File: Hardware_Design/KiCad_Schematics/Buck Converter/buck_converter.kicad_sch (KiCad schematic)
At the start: 3 parts, among them J1 Conn_01x02_Socket, J2 Conn_01x02_Socket, J3 Conn_01x01_Pin

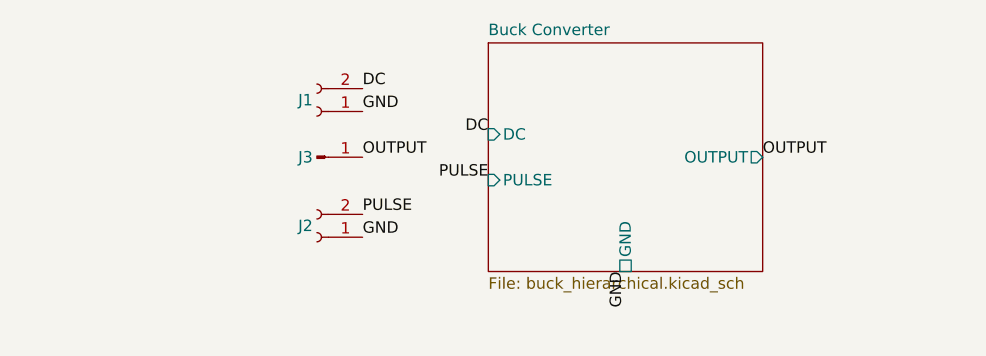
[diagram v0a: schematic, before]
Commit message: Add simulation circuit for Buck Converter
Added the simulation circuit to analyze the output graphs, but the expected waveform/results are not yet achieved.
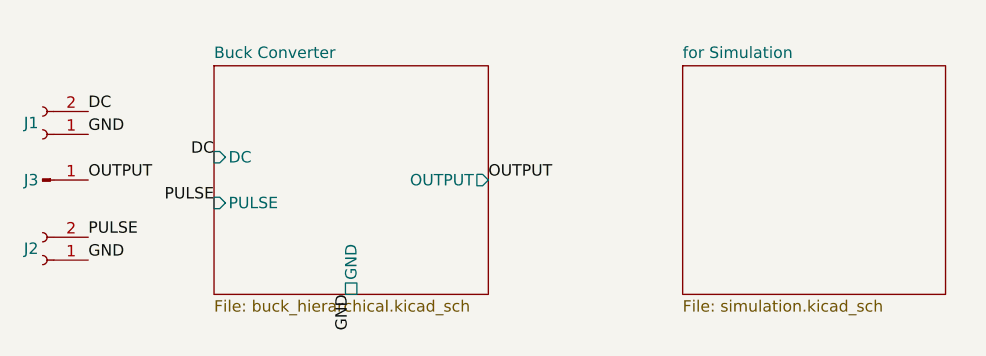
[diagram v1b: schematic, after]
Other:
- added sheet for Simulation (simulation.kicad_sch)
- moved on the sheet: J1, J2, J3
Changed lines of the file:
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@@
 	(paper "A4")
 	(label "GND"
-		(at 111.76 96.52 0)
+		(at 81.28 99.06 0)
 		(effects
 			(font
@@
 	)
 	(label "OUTPUT"
-		(at 111.76 101.6 0)
+		(at 81.28 104.14 0)
 		(effects
 			(font
@@
 	)
 	(label "GND"
-		(at 140.97 114.3 270)
+		(at 110.49 116.84 270)
 		(effects
 			(font
@@
 	)
 	(label "DC"
-		(at 111.76 93.98 0)
+		(at 81.28 96.52 0)
 		(effects
 			(font
@@
 	)
 	(label "PULSE"
-		(at 111.76 107.95 0)
+		(at 81.28 110.49 0)
 		(effects
 			(font
@@
 	)
 	(label "GND"
-		(at 111.76 110.49 0)
+		(at 81.28 113.03 0)
 		(effects
 			(font
@@
 	)
 	(label "OUTPUT"
-		(at 156.21 101.6 0)
+		(at 125.73 104.14 0)
 		(effects
 			(font
@@
 	)
 	(label "DC"
-		(at 125.73 99.06 180)
+		(at 95.25 101.6 180)
 		(effects
 			(font
@@
 	)
 	(label "PULSE"
-		(at 125.73 104.14 180)
+		(at 95.25 106.68 180)
 		(effects
 			(font
@@
 	(symbol
 		(lib_id "Connector:Conn_01x02_Socket")
-		(at 106.68 96.52 180)
+		(at 76.2 99.06 180)
 		(unit 1)
 		(body_style 1)
@@
 		(dnp no)
 		(property "Reference" "J1"
-			(at 105.41 95.25 0)
+			(at 74.93 97.79 0)
 			(show_name no)
 			(do_not_autoplace no)
@@
 		)
 		(property "Value" "Conn_01x02_Socket"
-			(at 107.315 91.44 0)
+			(at 76.835 93.98 0)
 			(hide yes)
 			(show_name no)
@@
 		)
 		(property "Footprint" "Connector_PinSocket_2.54mm:PinSocket_1x02_P2.54mm_Vertical"
-			(at 106.68 96.52 0)
+			(at 76.2 99.06 0)
 			(hide yes)
 			(show_name no)
@@
 		)
 		(property "Datasheet" ""
-			(at 106.68 96.52 0)
+			(at 76.2 99.06 0)
 			(hide yes)
 			(show_name no)
@@
 		)
 		(property "Description" "Generic connector, single row, 01x02, script generated"
-			(at 106.68 96.52 0)
+			(at 76.2 99.06 0)
 			(hide yes)
 			(show_name no)
@@
 	(symbol
 		(lib_id "Connector:Conn_01x01_Pin")
-		(at 106.68 101.6 0)
+		(at 76.2 104.14 0)
 		(unit 1)
 		(body_style 1)
@@
 		(dnp no)
 		(property "Reference" "J3"
-			(at 105.41 101.6 0)
+			(at 74.93 104.14 0)
 			(show_name no)
 			(do_not_autoplace no)
@@
 		)
 		(property "Value" "Conn_01x01_Pin"
-			(at 107.315 99.06 0)
+			(at 76.835 101.6 0)
 			(hide yes)
 			(show_name no)
@@
 		)
 		(property "Footprint" "Connector_PinHeader_2.54mm:PinHeader_1x01_P2.54mm_Vertical"
-			(at 106.68 101.6 0)
+			(at 76.2 104.14 0)
 			(hide yes)
 			(show_name no)
@@
 		)
 		(property "Datasheet" ""
-			(at 106.68 101.6 0)
+			(at 76.2 104.14 0)
 			(hide yes)
 			(show_name no)
@@
 		)
 		(property "Description" "Generic connector, single row, 01x01, script generated"
-			(at 106.68 101.6 0)
+			(at 76.2 104.14 0)
 			(hide yes)
 			(show_name no)
@@
 	(symbol
 		(lib_id "Connector:Conn_01x02_Socket")
-		(at 106.68 110.49 180)
+		(at 76.2 113.03 180)
 		(unit 1)
 		(body_style 1)
@@
 		(dnp no)
 		(property "Reference" "J2"
-			(at 105.41 109.22 0)
+			(at 74.93 111.76 0)
 			(show_name no)
 			(do_not_autoplace no)
@@
 		)
 		(property "Value" "Conn_01x02_Socket"
-			(at 107.315 105.41 0)
+			(at 76.835 107.95 0)
 			(hide yes)
 			(show_name no)
@@
 		)
 		(property "Footprint" "Connector_PinSocket_2.54mm:PinSocket_1x02_P2.54mm_Vertical"
-			(at 106.68 110.49 0)
+			(at 76.2 113.03 0)
 			(hide yes)
 			(show_name no)
@@
 		)
 		(property "Datasheet" ""
-			(at 106.68 110.49 0)
+			(at 76.2 113.03 0)
 			(hide yes)
 			(show_name no)
@@
 		)
 		(property "Description" "Generic connector, single row, 01x02, script generated"
-			(at 106.68 110.49 0)
+			(at 76.2 113.03 0)
 			(hide yes)
 			(show_name no)
@@
 	)
 	(sheet
-		(at 125.73 88.9)
+		(at 147.32 91.44)
+		(size 29.21 25.4)
+		(exclude_from_sim no)
+		(in_bom no)
+		(on_board no)
+		(dnp no)
+		(fields_autoplaced yes)
+		(stroke
+			(width 0.1524)
+			(type solid)
+			(color 194 0 0 1)
+		)
+		(fill
+			(color 0 0 0 0)
+		)
+		(property "Sheetname" "for Simulation"
+			(at 147.32 90.7284 0)
+			(show_name no)
+			(do_not_autoplace no)
+			(effects
+				(font
+					(size 1.27 1.27)
+				)
+				(justify left bottom)
+			)
+		)
+		(property "Sheetfile" "simulation.kicad_sch"
+			(at 147.32 117.4246 0)
+			(show_name no)
+			(do_not_autoplace no)
+			(effects
+				(font
+					(size 1.27 1.27)
+				)
+				(justify left top)
+			)
+		)
+		(instances
+			(project "buck_converter"
+				(path "/e6ad1407-9765-4ff4-965d-dd4ca2472230"
+					(page "3")
+				)
+			)
+		)
+	)
+	(sheet
+		(at 95.25 91.44)
 		(size 30.48 25.4)
 		(exclude_from_sim no)
@@
 		)
 		(property "Sheetname" "Buck Converter"
-			(at 125.73 88.1884 0)
+			(at 95.25 90.7284 0)
 			(show_name no)
 			(do_not_autoplace no)
@@
 		)
 		(property "Sheetfile" "buck_hierarchical.kicad_sch"
-			(at 125.73 114.8846 0)
+			(at 95.25 117.4246 0)
 			(show_name no)
 			(do_not_autoplace no)
@@
 		)
 		(pin "DC" input
-			(at 125.73 99.06 180)
+			(at 95.25 101.6 180)
 			(effects
 				(font
@@
 		)
 		(pin "OUTPUT" output
-			(at 156.21 101.6 0)
+			(at 125.73 104.14 0)
 			(effects
 				(font
@@
 		)
 		(pin "PULSE" input
-			(at 125.73 104.14 180)
+			(at 95.25 106.68 180)
 			(effects
 				(font
@@
 		)
 		(pin "GND" passive
-			(at 140.97 114.3 270)
-			(effects
-				(font
+			(at 110.49 116.84 270)
+			(effects
+				(font

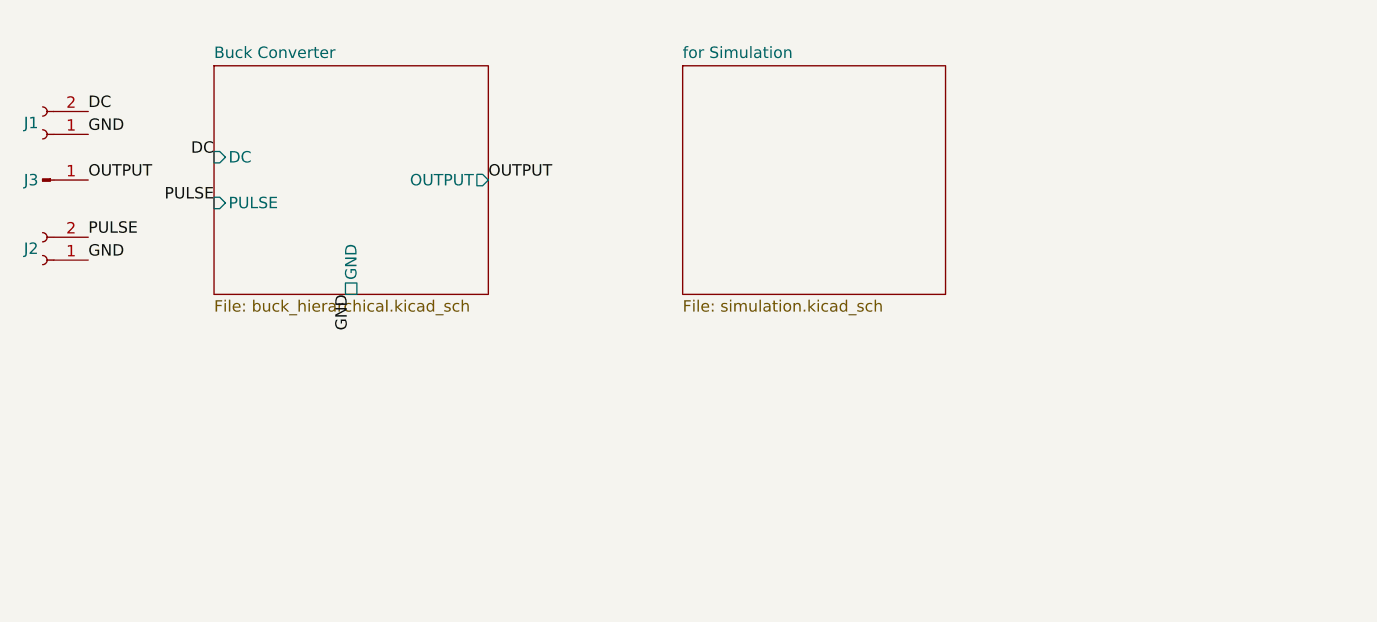
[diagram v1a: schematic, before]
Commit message: init: initialize new circuit for the previous problem
Started the Bootstrap Driver circuit to solve the previous problem. This way, the NMOSFET will be able to operate in full saturation.
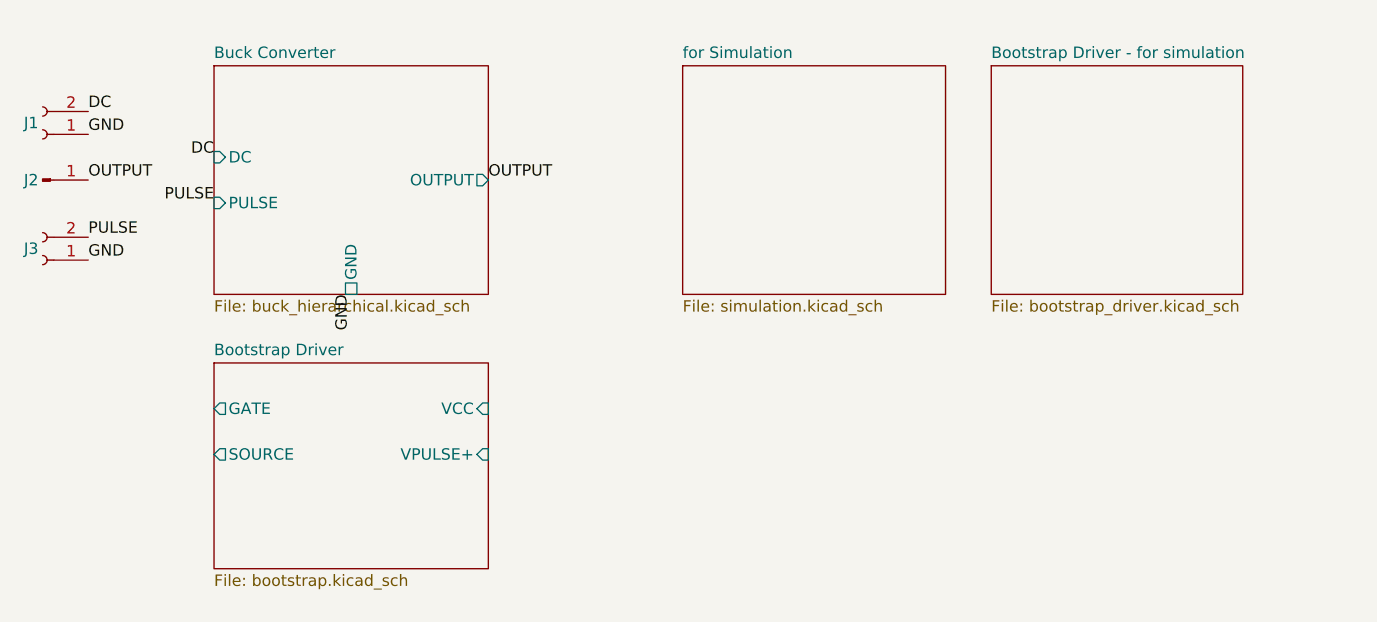
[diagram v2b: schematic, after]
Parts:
- renumbered J3 to J2, J2 to J3
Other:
- added sheet Bootstrap Driver (bootstrap.kicad_sch)
- added sheet Bootstrap Driver - for simulation (bootstrap_driver.kicad_sch)
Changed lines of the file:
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@@
 		(unit 1)
 		(body_style 1)
-		(exclude_from_sim no)
+		(exclude_from_sim yes)
 		(in_bom yes)
 		(on_board yes)
@@
 		(unit 1)
 		(body_style 1)
-		(exclude_from_sim no)
+		(exclude_from_sim yes)
 		(in_bom yes)
 		(on_board yes)
 		(in_pos_files yes)
 		(dnp no)
-		(property "Reference" "J3"
+		(property "Reference" "J2"
 			(at 74.93 104.14 0)
 			(show_name no)
@@
 			(project "buck_converter"
 				(path "/e6ad1407-9765-4ff4-965d-dd4ca2472230"
-					(reference "J3")
+					(reference "J2")
 					(unit 1)
 				)
@@
 		(unit 1)
 		(body_style 1)
+		(exclude_from_sim yes)
+		(in_bom yes)
+		(on_board yes)
+		(in_pos_files yes)
+		(dnp no)
+		(property "Reference" "J3"
+			(at 74.93 111.76 0)
+			(show_name no)
+			(do_not_autoplace no)
+			(effects
+				(font
+					(size 1.27 1.27)
+				)
+			)
+		)
+		(property "Value" "Conn_01x02_Socket"
+			(at 76.835 107.95 0)
+			(hide yes)
+			(show_name no)
+			(do_not_autoplace no)
+			(effects
+				(font
+					(size 1.27 1.27)
+				)
+			)
+		)
+		(property "Footprint" "Connector_PinSocket_2.54mm:PinSocket_1x02_P2.54mm_Vertical"
+			(at 76.2 113.03 0)
+			(hide yes)
+			(show_name no)
+			(do_not_autoplace no)
+			(effects
+				(font
+					(size 1.27 1.27)
+				)
+			)
+		)
+		(property "Datasheet" ""
+			(at 76.2 113.03 0)
+			(hide yes)
+			(show_name no)
+			(do_not_autoplace no)
+			(effects
+				(font
+					(size 1.27 1.27)
+				)
+			)
+		)
+		(property "Description" "Generic connector, single row, 01x02, script generated"
+			(at 76.2 113.03 0)
+			(hide yes)
+			(show_name no)
+			(do_not_autoplace no)
+			(effects
+				(font
+					(size 1.27 1.27)
+				)
+			)
+		)
+		(pin "2"
+		)
+		(pin "1"
+		)
+		(instances
+			(project "buck_converter"
+				(path "/e6ad1407-9765-4ff4-965d-dd4ca2472230"
+					(reference "J3")
+					(unit 1)
+				)
+			)
+		)
+	)
+	(sheet
+		(at 181.61 91.44)
+		(size 27.94 25.4)
 		(exclude_from_sim no)
 		(in_bom yes)
 		(on_board yes)
-		(in_pos_files yes)
-		(dnp no)
-		(property "Reference" "J2"
-			(at 74.93 111.76 0)
-			(show_name no)
-			(do_not_autoplace no)
-			(effects
-				(font
-					(size 1.27 1.27)
-				)
-			)
-		)
-		(property "Value" "Conn_01x02_Socket"
-			(at 76.835 107.95 0)
-			(hide yes)
-			(show_name no)
-			(do_not_autoplace no)
-			(effects
-				(font
-					(size 1.27 1.27)
-				)
-			)
-		)
-		(property "Footprint" "Connector_PinSocket_2.54mm:PinSocket_1x02_P2.54mm_Vertical"
-			(at 76.2 113.03 0)
-			(hide yes)
-			(show_name no)
-			(do_not_autoplace no)
-			(effects
-				(font
-					(size 1.27 1.27)
-				)
-			)
-		)
-		(property "Datasheet" ""
-			(at 76.2 113.03 0)
-			(hide yes)
-			(show_name no)
-			(do_not_autoplace no)
-			(effects
-				(font
-					(size 1.27 1.27)
-				)
-			)
-		)
-		(property "Description" "Generic connector, single row, 01x02, script generated"
-			(at 76.2 113.03 0)
-			(hide yes)
-			(show_name no)
-			(do_not_autoplace no)
-			(effects
-				(font
-					(size 1.27 1.27)
-				)
-			)
-		)
-		(pin "2"
-		)
-		(pin "1"
-		)
-		(instances
-			(project "buck_converter"
-				(path "/e6ad1407-9765-4ff4-965d-dd4ca2472230"
-					(reference "J2")
-					(unit 1)
+		(dnp no)
+		(fields_autoplaced yes)
+		(stroke
+			(width 0.1524)
+			(type solid)
+			(color 0 255 0 1)
+		)
+		(fill
+			(color 0 0 0 0)
+		)
+		(property "Sheetname" "Bootstrap Driver - for simulation"
+			(at 181.61 90.7284 0)
+			(show_name no)
+			(do_not_autoplace no)
+			(effects
+				(font
+					(size 1.27 1.27)
+				)
+				(justify left bottom)
+			)
+		)
+		(property "Sheetfile" "bootstrap_driver.kicad_sch"
+			(at 181.61 117.4246 0)
+			(show_name no)
+			(do_not_autoplace no)
+			(effects
+				(font
+					(size 1.27 1.27)
+				)
+				(justify left top)
+			)
+		)
+		(instances
+			(project "buck_converter"
+				(path "/e6ad1407-9765-4ff4-965d-dd4ca2472230"
+					(page "4")
 				)
 			)
@@
 			(width 0.1524)
 			(type solid)
-			(color 194 0 0 1)
+			(color 0 132 0 1)
 		)
 		(fill
@@
 				(path "/e6ad1407-9765-4ff4-965d-dd4ca2472230"
 					(page "3")
+				)
+			)
+		)
+	)
+	(sheet
+		(at 95.25 124.46)
+		(size 30.48 22.86)
+		(exclude_from_sim yes)
+		(in_bom no)
+		(on_board yes)
+		(dnp no)
+		(fields_autoplaced yes)
+		(stroke
+			(width 0.1524)
+			(type solid)
+		)
+		(fill
+			(color 0 0 0 0)
+		)
+		(property "Sheetname" "Bootstrap Driver"
+			(at 95.25 123.7484 0)
+			(show_name no)
+			(do_not_autoplace no)
+			(effects
+				(font
+					(size 1.27 1.27)
+				)
+				(justify left bottom)
+			)
+		)
+		(property "Sheetfile" "bootstrap.kicad_sch"
+			(at 95.25 147.9046 0)
+			(show_name no)
+			(do_not_autoplace no)
+			(effects
+				(font
+					(size 1.27 1.27)
+				)
+				(justify left top)
+			)
+		)
+		(pin "GATE" output
+			(at 95.25 129.54 180)
+			(effects
+				(font
+					(size 1.27 1.27)
+				)
+				(justify left)
+			)
+		)
+		(pin "SOURCE" output
+			(at 95.25 134.62 180)
+			(effects
+				(font
+					(size 1.27 1.27)
+				)
+				(justify left)
+			)
+		)
+		(pin "VCC" input
+			(at 125.73 129.54 0)
+			(effects
+				(font
+					(size 1.27 1.27)
+				)
+				(justify right)
+			)
+		)
+		(pin "VPULSE+" input
+			(at 125.73 134.62 0)
+			(effects
+				(font
+					(size 1.27 1.27)
+				)
+				(justify right)
+			)
+		)
+		(instances
+			(project "buck_converter"
+				(path "/e6ad1407-9765-4ff4-965d-dd4ca2472230"
+					(page "5")
 				)
 			)
@@
 		(at 95.25 91.44)
 		(size 30.48 25.4)
-		(exclude_from_sim no)
+		(exclude_from_sim yes)
 		(in_bom yes)
 		(on_board yes)
